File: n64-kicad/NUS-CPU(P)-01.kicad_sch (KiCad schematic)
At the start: 2 parts

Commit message: Rename files
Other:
- note added: "NUS-CPU(P)-01"
- note removed: "NUS-CPU-(P)-01"
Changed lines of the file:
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@@
     (effects (font (size 5.08 5.08)) (justify left bottom))
   )
-  (text "NUS-CPU-(P)-01" (at 45.72 25.4 0)
+  (text "NUS-CPU(P)-01" (at 45.72 25.4 0)
     (effects (font (size 5.08 5.08)) (justify left bottom))
   )
@@
           (reference "#PWR03") (unit 1)
         )
+        (path "/62362fc5-d8b0-453c-8cf3-9bf5adb1c5ec/2087c345-615f-4492-b530-065219fa6c1e"
+          (reference "#PWR07") (unit 1)
+        )
+        (path "/62362fc5-d8b0-453c-8cf3-9bf5adb1c5ec/fe0f5ce9-be45-40ad-8b42-2b325418535e"
+          (reference "#PWR011") (unit 1)
+        )
         (path "/62362fc5-d8b0-453c-8cf3-9bf5adb1c5ec/702eb8d5-895e-4c34-90ce-20d99f2fa9dd"
           (reference "#PWR03") (unit 1)
-        )
-        (path "/62362fc5-d8b0-453c-8cf3-9bf5adb1c5ec/2087c345-615f-4492-b530-065219fa6c1e"
-          (reference "#PWR07") (unit 1)
         )
       )
@@
           (reference "#PWR04") (unit 1)
         )
+        (path "/62362fc5-d8b0-453c-8cf3-9bf5adb1c5ec/2087c345-615f-4492-b530-065219fa6c1e"
+          (reference "#PWR08") (unit 1)
+        )
+        (path "/62362fc5-d8b0-453c-8cf3-9bf5adb1c5ec/fe0f5ce9-be45-40ad-8b42-2b325418535e"
+          (reference "#PWR012") (unit 1)
+        )
         (path "/62362fc5-d8b0-453c-8cf3-9bf5adb1c5ec/702eb8d5-895e-4c34-90ce-20d99f2fa9dd"
           (reference "#PWR04") (unit 1)
-        )
-        (path "/62362fc5-d8b0-453c-8cf3-9bf5adb1c5ec/2087c345-615f-4492-b530-065219fa6c1e"
-          (reference "#PWR08") (unit 1)
         )
       )
@@
           (reference "#PWR02") (unit 1)
         )
+        (path "/62362fc5-d8b0-453c-8cf3-9bf5adb1c5ec/2087c345-615f-4492-b530-065219fa6c1e"
+          (reference "#PWR06") (unit 1)
+        )
+        (path "/62362fc5-d8b0-453c-8cf3-9bf5adb1c5ec/fe0f5ce9-be45-40ad-8b42-2b325418535e"
+          (reference "#PWR010") (unit 1)
+        )
         (path "/62362fc5-d8b0-453c-8cf3-9bf5adb1c5ec/702eb8d5-895e-4c34-90ce-20d99f2fa9dd"
           (reference "#PWR02") (unit 1)
-        )
-        (path "/62362fc5-d8b0-453c-8cf3-9bf5adb1c5ec/2087c345-615f-4492-b530-065219fa6c1e"
-          (reference "#PWR06") (unit 1)
         )
       )
@@
           (reference "U1") (unit 1)
         )
+        (path "/62362fc5-d8b0-453c-8cf3-9bf5adb1c5ec/2087c345-615f-4492-b530-065219fa6c1e"
+          (reference "U3") (unit 1)
+        )
+        (path "/62362fc5-d8b0-453c-8cf3-9bf5adb1c5ec/fe0f5ce9-be45-40ad-8b42-2b325418535e"
+          (reference "U6") (unit 1)
+        )
         (path "/62362fc5-d8b0-453c-8cf3-9bf5adb1c5ec/702eb8d5-895e-4c34-90ce-20d99f2fa9dd"
           (reference "U1") (unit 1)
-        )
-        (path "/62362fc5-d8b0-453c-8cf3-9bf5adb1c5ec/2087c345-615f-4492-b530-065219fa6c1e"
-          (reference "U3") (unit 1)
         )
       )
@@
           (reference "U4") (unit 1)
         )
+        (path "/62362fc5-d8b0-453c-8cf3-9bf5adb1c5ec/2087c345-615f-4492-b530-065219fa6c1e"
+          (reference "U4") (unit 1)
+        )
+        (path "/62362fc5-d8b0-453c-8cf3-9bf5adb1c5ec/fe0f5ce9-be45-40ad-8b42-2b325418535e"
+          (reference "U7") (unit 1)
+        )
         (path "/62362fc5-d8b0-453c-8cf3-9bf5adb1c5ec/702eb8d5-895e-4c34-90ce-20d99f2fa9dd"
           (reference "U2") (unit 1)
-        )
-        (path "/62362fc5-d8b0-453c-8cf3-9bf5adb1c5ec/2087c345-615f-4492-b530-065219fa6c1e"
-          (reference "U4") (unit 1)
         )
       )
@@
           (reference "#PWR01") (unit 1)
         )
+        (path "/62362fc5-d8b0-453c-8cf3-9bf5adb1c5ec/2087c345-615f-4492-b530-065219fa6c1e"
+          (reference "#PWR05") (unit 1)
+        )
+        (path "/62362fc5-d8b0-453c-8cf3-9bf5adb1c5ec/fe0f5ce9-be45-40ad-8b42-2b325418535e"
+          (reference "#PWR09") (unit 1)
+        )
         (path "/62362fc5-d8b0-453c-8cf3-9bf5adb1c5ec/702eb8d5-895e-4c34-90ce-20d99f2fa9dd"
           (reference "#PWR01") (unit 1)
         )
-        (path "/62362fc5-d8b0-453c-8cf3-9bf5adb1c5ec/2087c345-615f-4492-b530-065219fa6c1e"
-          (reference "#PWR05") (unit 1)
-        )
-      )
+      )

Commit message: Update
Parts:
- added U7: ~, symbol n64:PIF(P)-NUS
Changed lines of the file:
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@@
+    )
+  )
+  (symbol (lib_id "n64:PIF(P)-NUS") (at 262.89 199.39 0) (unit 1)
+    (in_bom yes) (on_board yes) (dnp no)
+    (property "Reference" "U7" (at 261.62 199.39 0)
+      (effects (font (size 1.27 1.27)))
+    )
+    (property "Value" "~" (at 262.89 199.39 0)
+      (effects (font (size 1.27 1.27)))
+    )
+    (property "Footprint" "" (at 262.89 199.39 0)
+      (effects (font (size 1.27 1.27)) hide)
+    )
+    (property "Datasheet" "" (at 262.89 199.39 0)
+      (effects (font (size 1.27 1.27)) hide)
+    )
+    (pin "1")
+    (pin "10")
+    (pin "11")
+    (pin "12")
+    (pin "13")
+    (pin "14")
+    (pin "15")
+    (pin "16")
+    (pin "17")
+    (pin "18")
+    (pin "19")
+    (pin "2")
+    (pin "20")
+    (pin "21")
+    (pin "22")
+    (pin "23")
+    (pin "24")
+    (pin "25")
+    (pin "26")
+    (pin "27")
+    (pin "28")
+    (pin "3")
+    (pin "4")
+    (pin "5")
+    (pin "6")
+    (pin "7")
+    (pin "8")
+    (pin "9")
+    (instances
+      (project "n64-kicad"
+        (path "/62362fc5-d8b0-453c-8cf3-9bf5adb1c5ec/702eb8d5-895e-4c34-90ce-20d99f2fa9dd"
+          (reference "U7") (unit 1)
+        )
+      )
     )
   )

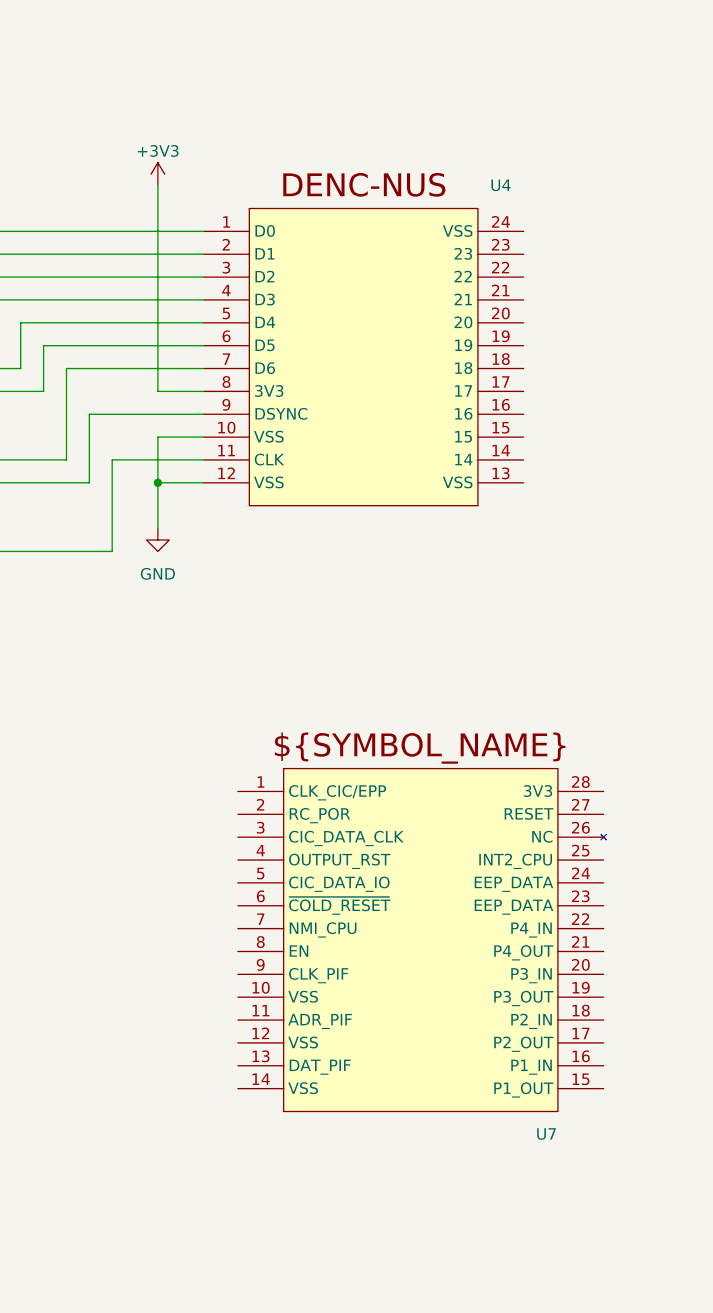
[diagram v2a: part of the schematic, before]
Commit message: Fix labels and update PDF
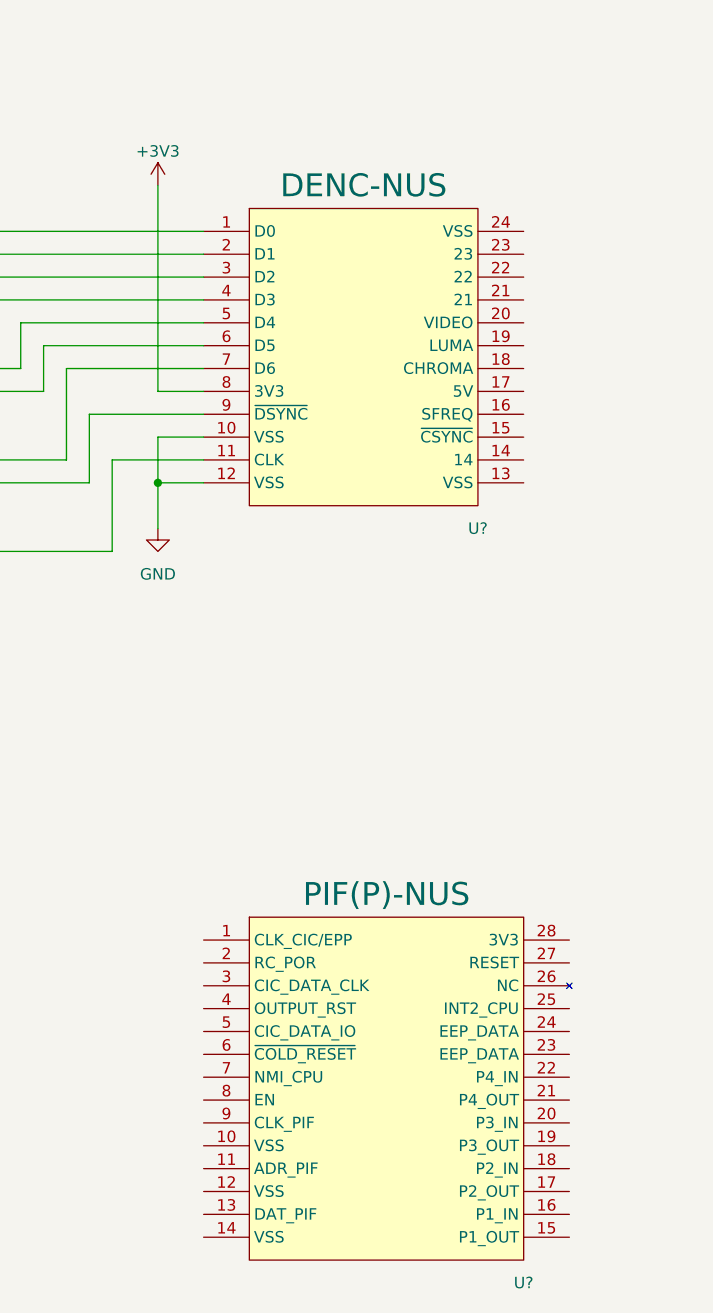
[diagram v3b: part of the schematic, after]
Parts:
- removed U4: ~, symbol n64:DENC-NUS
- removed U7: ~, symbol n64:PIF(P)-NUS
- added U?: PIF(P)-NUS, symbol n64:PIF(P)-NUS
- added U?: DENC-NUS, symbol n64:DENC-NUS
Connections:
- net +3V3: now also U?.8 (3V3)
- net GND: now also U?.10 (VSS), U?.12 (VSS)
- net at U1.11 (VIDEO_CLK): now also U?.11 (CLK)
- net at U1.14 (VIDEO_SYNC): now also U?.9 (~{DSYNC})
- net at U1.15 (VIDEO_D6): now also U?.7 (D6)
- net at U1.18 (VIDEO_D5): now also U?.6 (D5)
- net at U1.19 (VIDEO_D4): now also U?.5 (D4)
- net at U1.20 (VIDEO_D3): now also U?.4 (D3)
- net at U1.23 (VIDEO_D2): now also U?.3 (D2)
- net at U1.24 (VIDEO_D1): now also U?.2 (D1)
- net at U1.25 (VIDEO_D0): now also U?.1 (D0)
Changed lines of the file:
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@@
+    )
+  )
+  (symbol (lib_id "n64:PIF(P)-NUS") (at 259.08 215.9 0) (unit 1)
+    (in_bom yes) (on_board yes) (dnp no) (fields_autoplaced)
+    (property "Reference" "U?" (at 259.08 215.9 0) (do_not_autoplace)
+      (effects (font (size 1.27 1.27)))
+    )
+    (property "Value" "PIF(P)-NUS" (at 243.84 172.72 0) (do_not_autoplace)
+      (effects (font (size 2.54 2.54)))
+    )
+    (property "Footprint" "" (at 259.08 215.9 0)
+      (effects (font (size 1.27 1.27)) hide)
+    )
+    (property "Datasheet" "" (at 259.08 215.9 0)
+      (effects (font (size 1.27 1.27)) hide)
+    )
+    (pin "1")
+    (pin "10")
+    (pin "11")
+    (pin "12")
+    (pin "13")
+    (pin "14")
+    (pin "15")
+    (pin "16")
+    (pin "17")
+    (pin "18")
+    (pin "19")
+    (pin "2")
+    (pin "20")
+    (pin "21")
+    (pin "22")
+    (pin "23")
+    (pin "24")
+    (pin "25")
+    (pin "26")
+    (pin "27")
+    (pin "28")
+    (pin "3")
+    (pin "4")
+    (pin "5")
+    (pin "6")
+    (pin "7")
+    (pin "8")
+    (pin "9")
+    (instances
+      (project "n64-kicad"
+        (path "/62362fc5-d8b0-453c-8cf3-9bf5adb1c5ec/702eb8d5-895e-4c34-90ce-20d99f2fa9dd"
+          (reference "U?") (unit 1)
+        )
+      )
     )
   )
@@
         )
         (path "/62362fc5-d8b0-453c-8cf3-9bf5adb1c5ec/702eb8d5-895e-4c34-90ce-20d99f2fa9dd"
-          (reference "U1") (unit 1)
+          (reference "U?") (unit 1)
+        )
+      )
+    )
+  )
+  (symbol (lib_id "power:GND") (at 162.56 180.34 0) (unit 1)
+    (in_bom yes) (on_board yes) (dnp no) (fields_autoplaced)
+    (property "Reference" "#PWR01" (at 162.56 186.69 0)
+      (effects (font (size 1.27 1.27)) hide)
+    )
+    (property "Value" "GND" (at 162.56 185.42 0)
+      (effects (font (size 1.27 1.27)))
+    )
+    (property "Footprint" "" (at 162.56 180.34 0)
+      (effects (font (size 1.27 1.27)) hide)
+    )
+    (property "Datasheet" "" (at 162.56 180.34 0)
+      (effects (font (size 1.27 1.27)) hide)
+    )
+    (pin "1")
+    (instances
+      (project "n64-kicad"
+        (path "/62362fc5-d8b0-453c-8cf3-9bf5adb1c5ec"
+          (reference "#PWR01") (unit 1)
+        )
+        (path "/62362fc5-d8b0-453c-8cf3-9bf5adb1c5ec/2087c345-615f-4492-b530-065219fa6c1e"
+          (reference "#PWR05") (unit 1)
+        )
+        (path "/62362fc5-d8b0-453c-8cf3-9bf5adb1c5ec/fe0f5ce9-be45-40ad-8b42-2b325418535e"
+          (reference "#PWR09") (unit 1)
+        )
+        (path "/62362fc5-d8b0-453c-8cf3-9bf5adb1c5ec/702eb8d5-895e-4c34-90ce-20d99f2fa9dd"
+          (reference "#PWR01") (unit 1)
         )
       )
@@
   )
   (symbol (lib_id "n64:DENC-NUS") (at 256.54 132.08 0) (unit 1)
-    (in_bom yes) (on_board yes) (dnp no)
-    (property "Reference" "U4" (at 256.54 93.98 0)
-      (effects (font (size 1.27 1.27)))
-    )
-    (property "Value" "~" (at 228.6 96.52 0)
-      (effects (font (size 1.27 1.27)))
+    (in_bom yes) (on_board yes) (dnp no) (fields_autoplaced)
+    (property "Reference" "U?" (at 254 132.08 0) (do_not_autoplace)
+      (effects (font (size 1.27 1.27)))
+    )
+    (property "Value" "DENC-NUS" (at 241.3 93.98 0) (do_not_autoplace)
+      (effects (font (size 2.54 2.54)))
     )
     (property "Footprint" "" (at 228.6 96.52 0)
@@
     (instances
       (project "n64-kicad"
-        (path "/62362fc5-d8b0-453c-8cf3-9bf5adb1c5ec"
-          (reference "U4") (unit 1)
-        )
-        (path "/62362fc5-d8b0-453c-8cf3-9bf5adb1c5ec/2087c345-615f-4492-b530-065219fa6c1e"
-          (reference "U4") (unit 1)
-        )
-        (path "/62362fc5-d8b0-453c-8cf3-9bf5adb1c5ec/fe0f5ce9-be45-40ad-8b42-2b325418535e"
-          (reference "U7") (unit 1)
-        )
-        (path "/62362fc5-d8b0-453c-8cf3-9bf5adb1c5ec/702eb8d5-895e-4c34-90ce-20d99f2fa9dd"
-          (reference "U2") (unit 1)
-        )
-      )
-    )
-  )
-  (symbol (lib_id "n64:PIF(P)-NUS") (at 262.89 199.39 0) (unit 1)
-    (in_bom yes) (on_board yes) (dnp no)
-    (property "Reference" "U7" (at 261.62 199.39 0)
-      (effects (font (size 1.27 1.27)))
-    )
-    (property "Value" "~" (at 262.89 199.39 0)
-      (effects (font (size 1.27 1.27)))
-    )
-    (property "Footprint" "" (at 262.89 199.39 0)
-      (effects (font (size 1.27 1.27)) hide)
-    )
-    (property "Datasheet" "" (at 262.89 199.39 0)
-      (effects (font (size 1.27 1.27)) hide)
-    )
-    (pin "1")
-    (pin "10")
-    (pin "11")
-    (pin "12")
-    (pin "13")
-    (pin "14")
-    (pin "15")
-    (pin "16")
-    (pin "17")
-    (pin "18")
-    (pin "19")
-    (pin "2")
-    (pin "20")
-    (pin "21")
-    (pin "22")
-    (pin "23")
-    (pin "24")
-    (pin "25")
-    (pin "26")
-    (pin "27")
-    (pin "28")
-    (pin "3")
-    (pin "4")
-    (pin "5")
-    (pin "6")
-    (pin "7")
-    (pin "8")
-    (pin "9")
-    (instances
-      (project "n64-kicad"
-        (path "/62362fc5-d8b0-453c-8cf3-9bf5adb1c5ec/702eb8d5-895e-4c34-90ce-20d99f2fa9dd"
-          (reference "U7") (unit 1)
-        )
-      )
-    )
-  )
-  (symbol (lib_id "power:GND") (at 162.56 180.34 0) (unit 1)
-    (in_bom yes) (on_board yes) (dnp no) (fields_autoplaced)
-    (property "Reference" "#PWR01" (at 162.56 186.69 0)
-      (effects (font (size 1.27 1.27)) hide)
-    )
-    (property "Value" "GND" (at 162.56 185.42 0)
-      (effects (font (size 1.27 1.27)))
-    )
-    (property "Footprint" "" (at 162.56 180.34 0)
-      (effects (font (size 1.27 1.27)) hide)
-    )
-    (property "Datasheet" "" (at 162.56 180.34 0)
-      (effects (font (size 1.27 1.27)) hide)
-    )
-    (pin "1")
-    (instances
-      (project "n64-kicad"
-        (path "/62362fc5-d8b0-453c-8cf3-9bf5adb1c5ec"
-          (reference "#PWR01") (unit 1)
-        )
-        (path "/62362fc5-d8b0-453c-8cf3-9bf5adb1c5ec/2087c345-615f-4492-b530-065219fa6c1e"
-          (reference "#PWR05") (unit 1)
-        )
-        (path "/62362fc5-d8b0-453c-8cf3-9bf5adb1c5ec/fe0f5ce9-be45-40ad-8b42-2b325418535e"
-          (reference "#PWR09") (unit 1)
-        )
-        (path "/62362fc5-d8b0-453c-8cf3-9bf5adb1c5ec/702eb8d5-895e-4c34-90ce-20d99f2fa9dd"
-          (reference "#PWR01") (unit 1)
-        )
-      )
+        (path "/62362fc5-d8b0-453c-8cf3-9bf5adb1c5ec/702eb8d5-895e-4c34-90ce-20d99f2fa9dd"
+          (reference "U?") (unit 1)
+        )
+      )
